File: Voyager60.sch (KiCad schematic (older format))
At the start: 201 parts, among them SW1 5.2x5.2mm, U1 ATmega32U4-MU, U2 PRTR5V0U2X, Y1 16Mhz

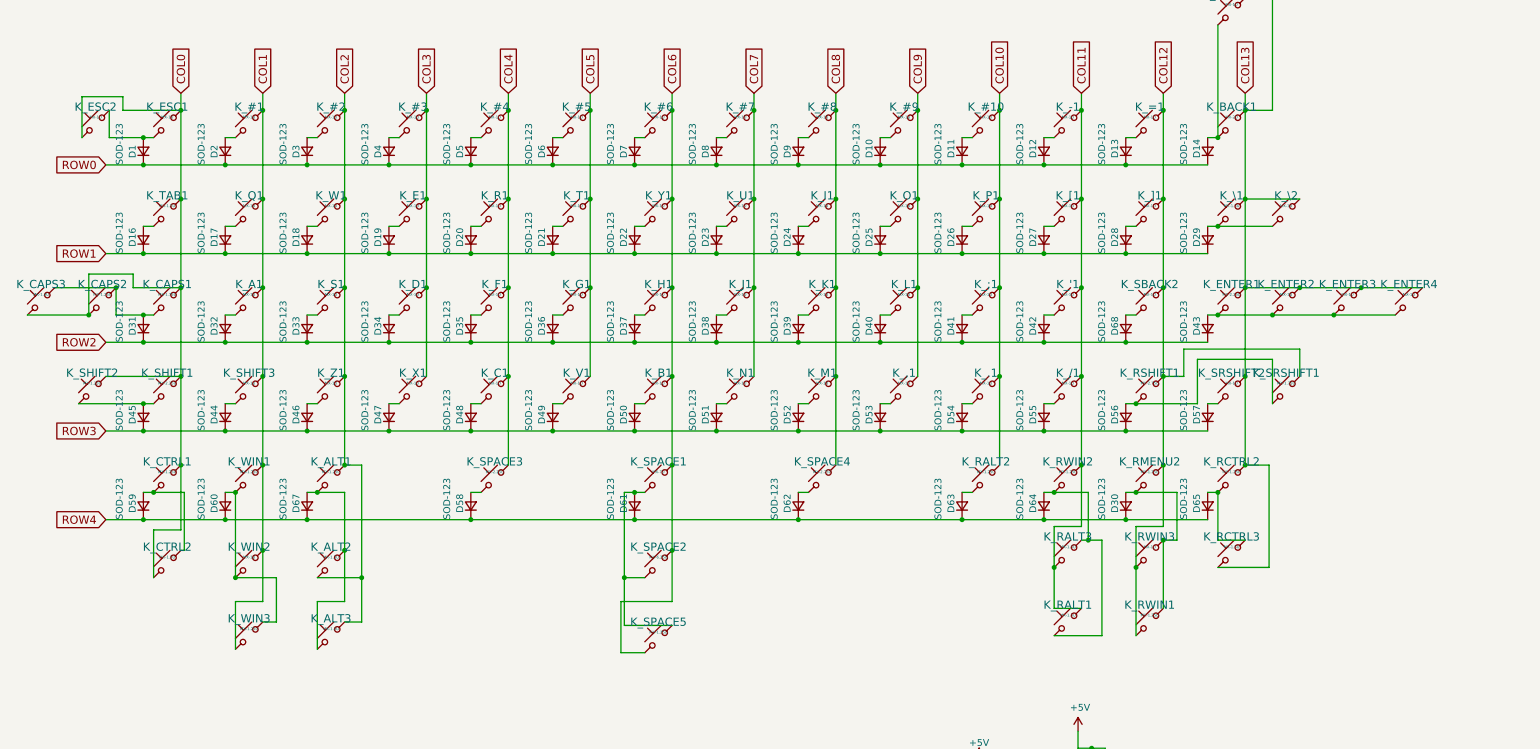
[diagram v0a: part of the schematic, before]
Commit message: Redo layout with SMK footprints
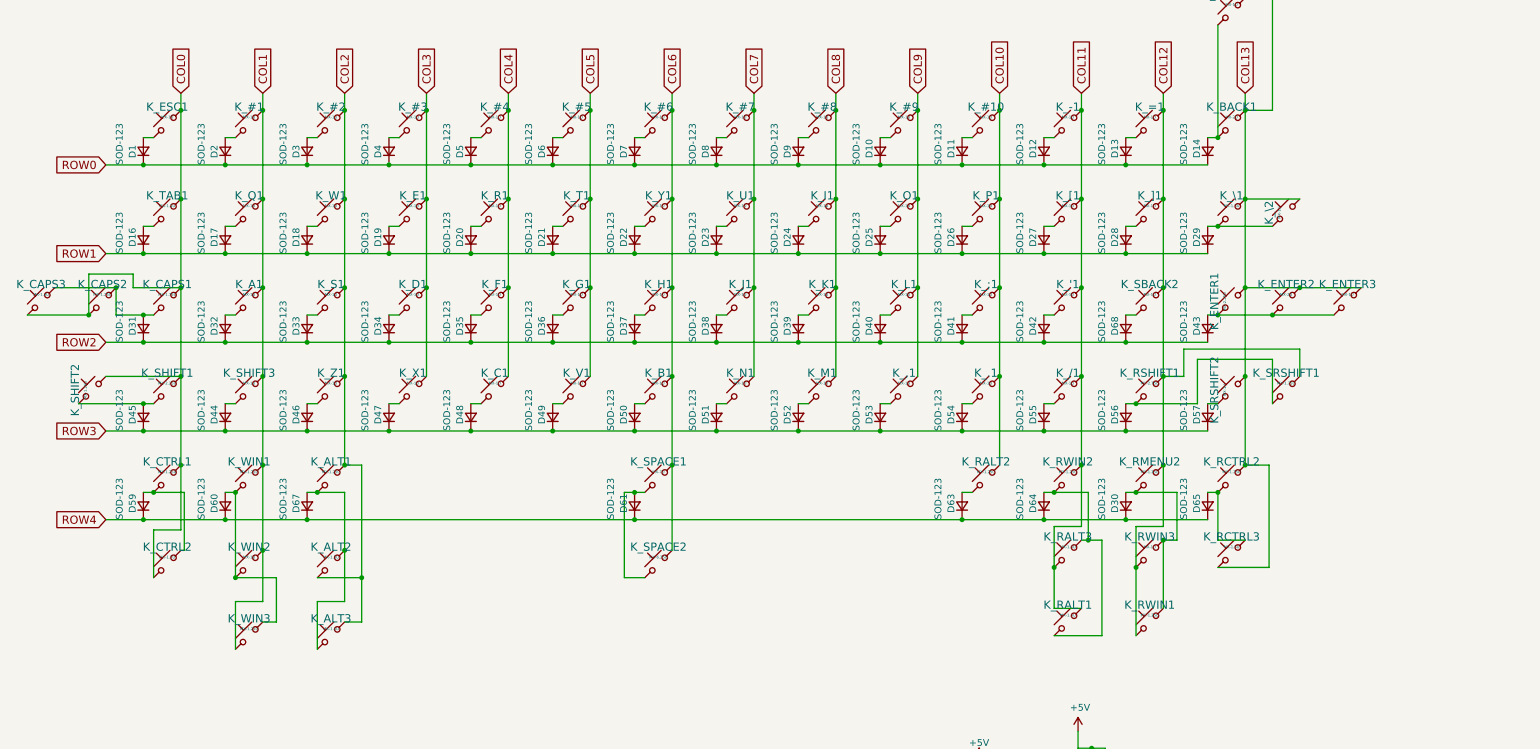
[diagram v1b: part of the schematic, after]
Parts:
- removed D58, D62: SOD-123, Diodes_SMD:D_SOD-123, symbol Device:D_Small
- removed K_ENTER4, K_ESC2: MX-1U, MX_Alps_Hybrid:ALPS-1U, symbol Switch:SW_Push_45deg
- removed K_SPACE3: MX-2.25U, MX_Alps_Hybrid:ALPS-2.25U, symbol Switch:SW_Push_45deg
- removed K_SPACE4: MX-2.75U, MX_Alps_Hybrid:ALPS-2.75U, symbol Switch:SW_Push_45deg
- removed K_SPACE5: MX-1.25U, MX_Alps_Hybrid:ALPS-1.25U, symbol Switch:SW_Push_45deg
- K_#1, K_#10, K_#2, K_#3, K_#4, K_#5, K_#6, K_#7, K_#8, K_#9, K_'1, K_,1, K_-1, K_.1, K_/1, K_;1, K_=1, K_A1, K_B1, K_C1, K_D1, K_E1, K_ENTER3, K_ESC1, K_F1, K_G1, K_H1, K_I1, K_J1, K_K1, K_L1, K_M1, K_N1, K_O1, K_P1, K_Q1, K_R1, K_RWIN3, K_S1, K_SBACK1, K_SBACK2, K_SHIFT3, K_SRSHIFT2, K_T1, K_U1, K_V1, K_W1, K_WIN2, K_X1, K_Y1, K_Z1, K_[1, K_\2, K_]1: footprint MX_Alps_Hybrid:ALPS-1U -> smk:SW_SMK
- K_ALT1, K_CAPS2, K_CTRL1, K_RALT2, K_RCTRL2, K_RMENU2, K_RWIN1, K_RWIN2, K_SHIFT2, K_WIN1, K_WIN3: footprint MX_Alps_Hybrid:ALPS-1.25U -> smk:SW_SMK
- K_ALT2, K_ALT3, K_CAPS3, K_CTRL2, K_RALT1, K_RALT3, K_RCTRL3, K_TAB1, K_\1: footprint MX_Alps_Hybrid:ALPS-1.5U -> smk:SW_SMK
- K_BACK1: footprint MX_Alps_Hybrid:ALPS-2U -> smk:SW_SMK_2u
- K_CAPS1, K_SRSHIFT1: footprint MX_Alps_Hybrid:ALPS-1.75U -> smk:SW_SMK
- K_ENTER1, K_SHIFT1: footprint MX_Alps_Hybrid:ALPS-2.25U -> smk:SW_SMK_2u
- K_ENTER2: value MX-1U -> MX-2U; footprint MX_Alps_Hybrid:ALPS-1U -> smk:SW_SMK_2u_R
- K_RSHIFT1: footprint MX_Alps_Hybrid:ALPS-2.75U -> smk:SW_SMK_2u
- K_SPACE1: footprint MX_Alps_Hybrid:ALPS-7U -> smk:SW_SMK_7u_R
- K_SPACE2: footprint MX_Alps_Hybrid:ALPS-6.25U -> smk:SW_SMK_6.25u_R
- SW1: footprint Molex-0548190589:SKQG-1155865 -> Button_Switch_SMD:SW_SPST_SKQG_WithStem
- U1: footprint Housings_DFN_QFN:QFN-44-1EP_7x7mm_Pitch0.5mm -> Package_DFN_QFN:QFN-44-1EP_7x7mm_P0.5mm_EP5.2x5.2mm
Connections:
- net COL0: now also K_SHIFT2.2; no longer K_SHIFT2.1
- net COL13: now also K_ENTER1.2, K_SRSHIFT2.2, K_\2.2; no longer K_ENTER1.1, K_SRSHIFT2.1, K_\2.1
- net at D29.2 (A), K_\1.2: now also K_\2.1; no longer K_\2.2
- net at D43.2 (A), K_ENTER2.2, K_ENTER3.2: now also K_ENTER1.1; no longer K_ENTER1.2
- net at D45.2 (A), K_SHIFT1.2: now also K_SHIFT2.1; no longer K_SHIFT2.2
- net at D57.2 (A): now also K_SRSHIFT2.1; no longer K_SRSHIFT2.2
